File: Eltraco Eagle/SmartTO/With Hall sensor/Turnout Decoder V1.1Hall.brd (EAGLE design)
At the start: 100 x 80 mm, 88 parts, among them K1 NA, K2 NA, T1 BC547, T2 BC547, T3 BC547, T4 BC547

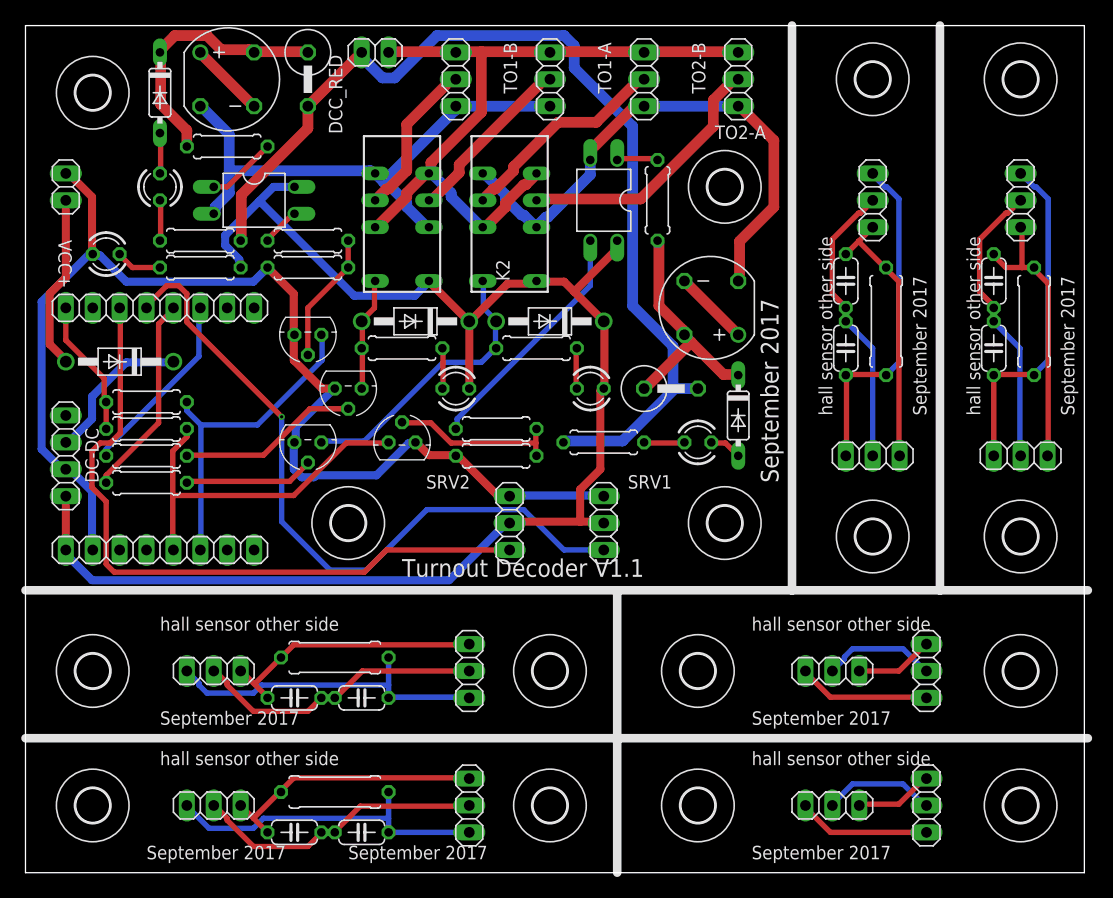
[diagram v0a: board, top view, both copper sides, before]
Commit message: New version PCB files and extra PCBs
Value of components printed on PCB. Current sensor, hall sensor and
relais add-on PCB added
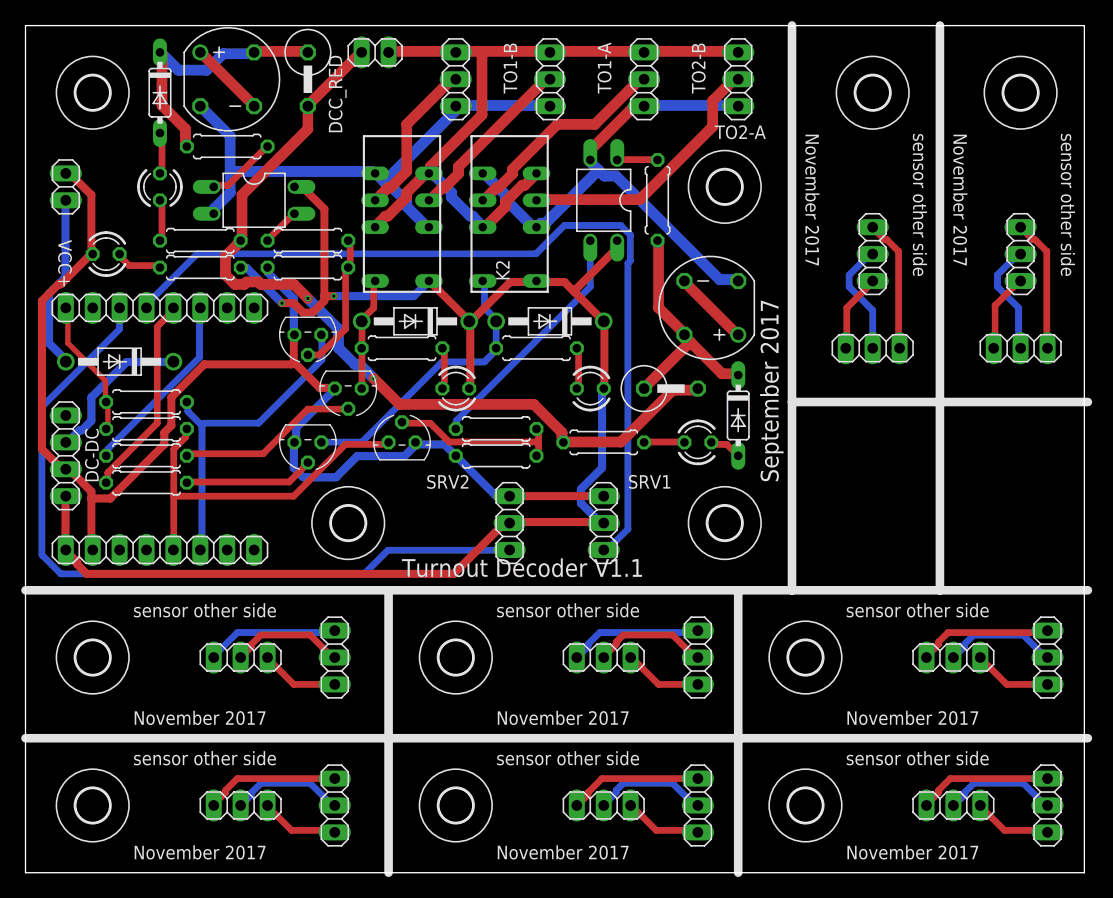
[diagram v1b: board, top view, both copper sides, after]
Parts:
- removed C1, C11, C12, C2, C4, C5, C6, C7: 10n, resistor:C050-024X044
- removed R12, R13, R15, R4: 10k, resistor:0309/10
- removed U$10, U$13, U$8, U$9: (no value), holes:3,2
- added HALL7, HALL8, JP7, JP8: (no value), pinhead:1X03
- moved U$7 68.9 mm to (73.7, 6.35), turned to 0 degrees
- moved U$5 67.3 mm to (73.7, 20.3)
- moved U$15 53.4 mm to (40.6, 20.3)
- moved U$16 53.3 mm to (40.6, 6.35)
- moved U$6 43.2 mm to (6.35, 20.3)
- moved U$14 43.2 mm to (6.35, 6.35)
- moved U$11 41.9 mm to (80.0, 73.7)
- moved U$12 41.9 mm to (94.0, 73.7)
- moved HALL5 21.6 mm to (54.6, 20.3), turned to 0 degrees
- moved JP2 21.6 mm to (63.5, 20.3)
- moved HALL6 21.6 mm to (54.6, 6.35), turned to 0 degrees
- moved JP3 21.6 mm to (63.5, 6.35)
- moved JP5 12.8 mm to (29.2, 20.3)
- moved JP1 12.7 mm to (29.2, 6.35)
- moved JP4 10.2 mm to (80.0, 49.5)
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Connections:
- new net N$52: HALL7.2, JP7.2
- new net N$53: HALL7.1, JP7.1
- new net N$54: HALL7.3, JP7.3
- new net N$59: HALL8.2, JP8.2
- new net N$60: HALL8.1, JP8.1
- new net N$61: HALL8.3, JP8.3
- net N$1: no longer C4.2, C5.1
- net N$24: no longer C5.2, R4.1
- net N$25: no longer C4.1, R4.2
- net N$30: no longer C6.2, C7.1
- net N$36: no longer C7.2, R12.1
- net N$37: no longer C6.1, R12.2
- net N$38: no longer C1.2, C2.1
- net N$39: no longer C2.2, R13.1
- net N$40: no longer C1.1, R13.2
- net N$55: no longer C11.2, C12.1
- net N$56: no longer C11.1, R15.2
- net N$57: no longer C12.2, R15.1
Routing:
- net N$37: track 32.3 -> 7.49 mm
- net N$56: track 32.2 -> 7.43 mm
- net N$25: track 31.8 -> 7.43 mm
- net N$40: track 31.8 -> 7.49 mm
- net N$38: track 27.5 -> 10.9 mm
- net N$1: track 27.4 -> 10.9 mm
- net N$30: track 27.5 -> 10.9 mm
- net N$55: track 27.5 -> 11.0 mm
- net N$3: track 97.0 -> 81.3 mm, vias 0 -> 2
- net N$36: track 26.7 -> 12.6 mm
- net N$31: track 66.6 -> 80.6 mm, vias 1 -> 0
- net N$39: track 25.7 -> 12.7 mm
- net N$24: track 25.5 -> 12.6 mm
- net N$57: track 25.5 -> 12.6 mm
- net N$54: track 0.00 -> 12.7 mm
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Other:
- board text added: "November 2017"
- board text added: "S"
- board text added: "sensor other side"
- board text removed: "hall sensor other side"
